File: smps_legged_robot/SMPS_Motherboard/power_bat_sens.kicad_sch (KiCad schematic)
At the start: 4 parts, among them IC2001 INA239AQDGSRQ1

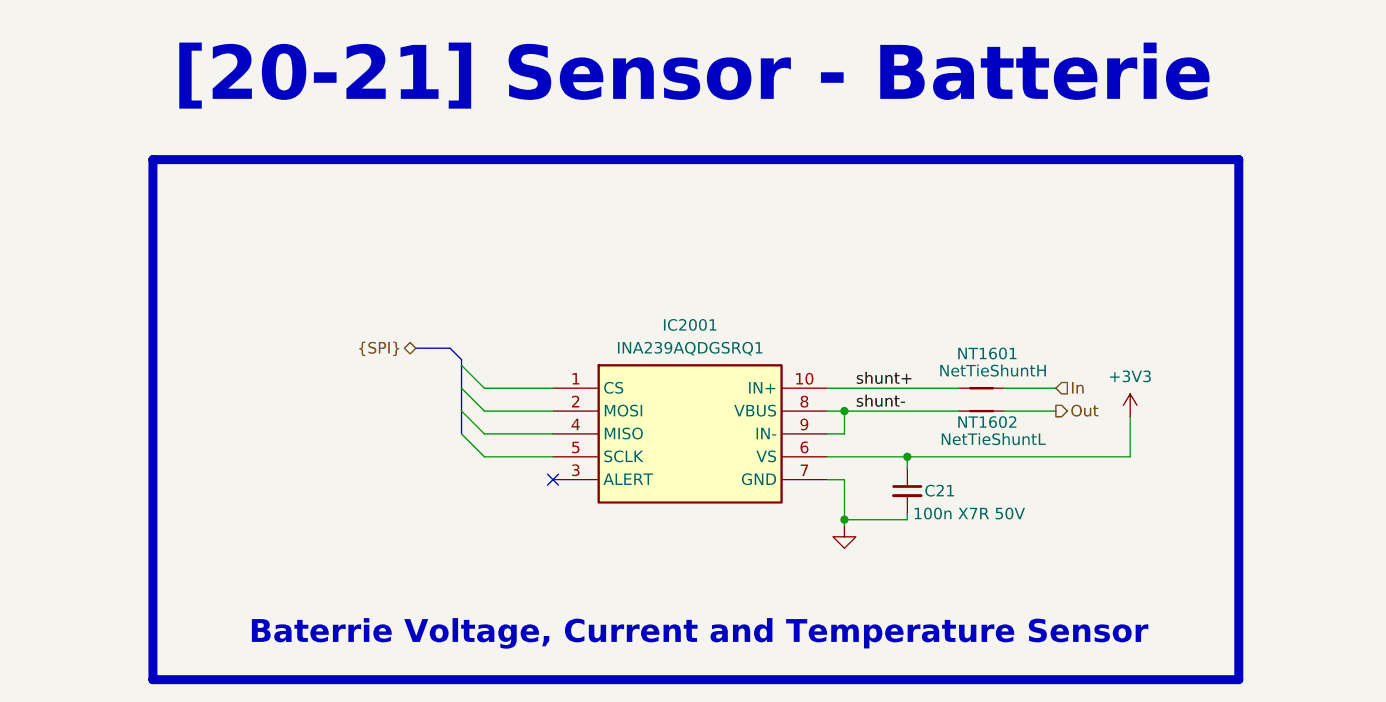
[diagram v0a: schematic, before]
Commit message: Rev 1.0 of smps finished -> waiting for verification
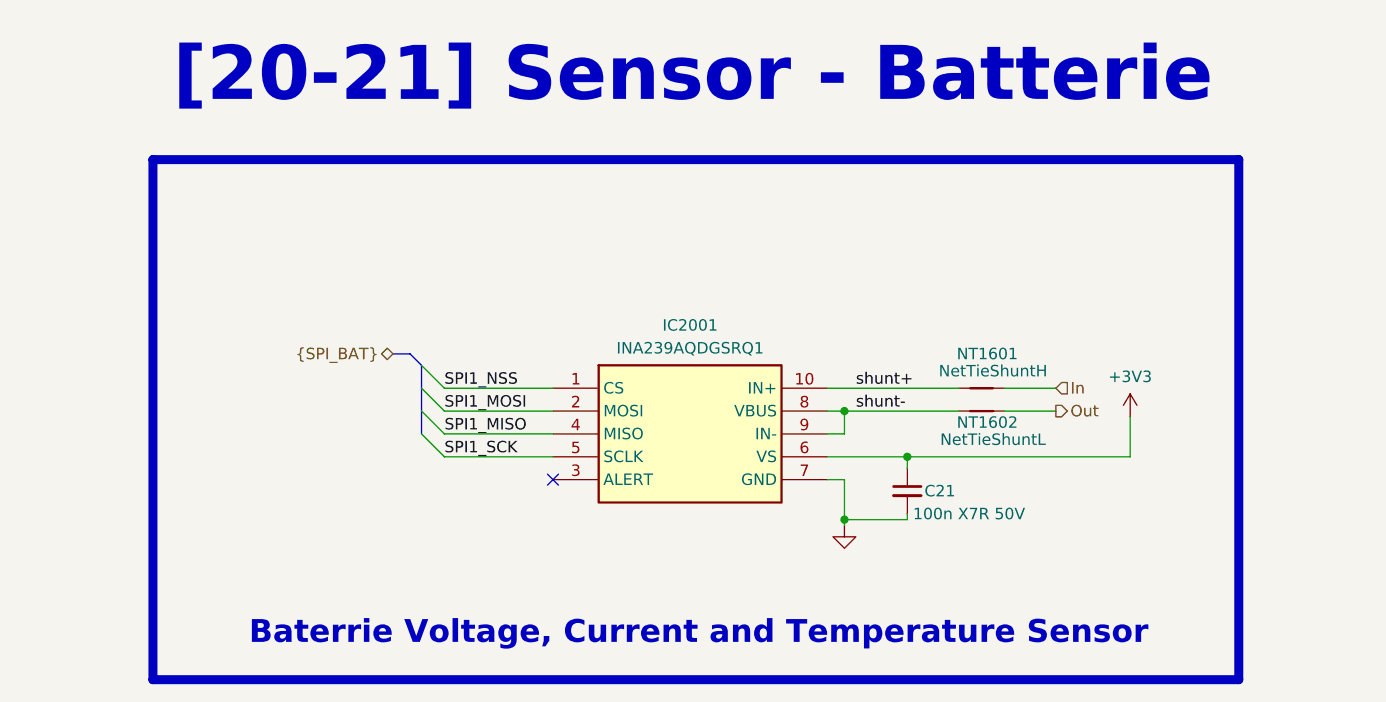
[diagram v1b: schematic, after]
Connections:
- net SPI1_NSS: now reaches IC2001.1 (CS)
- net SPI1_MOSI: now reaches IC2001.2 (MOSI)
- net SPI1_MISO: now reaches IC2001.4 (MISO)
- net SPI1_SCK: now reaches IC2001.5 (SCLK)
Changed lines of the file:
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@@
   )
   (no_connect (at 89.535 66.04))
-  (bus_entry (at 79.375 55.88) (size 2.54 2.54)
+  (bus_entry (at 74.93 53.34) (size 2.54 2.54)
     (stroke (width 0) (type default))
   )
-  (bus_entry (at 79.375 53.34) (size 2.54 2.54)
+  (bus_entry (at 74.93 60.96) (size 2.54 2.54)
     (stroke (width 0) (type default))
   )
-  (bus_entry (at 79.375 58.42) (size 2.54 2.54)
+  (bus_entry (at 74.93 58.42) (size 2.54 2.54)
     (stroke (width 0) (type default))
   )
-  (bus_entry (at 79.375 60.96) (size 2.54 2.54)
+  (bus_entry (at 74.93 55.88) (size 2.54 2.54)
     (stroke (width 0) (type default))
   )
@@
     (stroke (width 0) (type default))
   )
-  (bus (pts (xy 79.375 52.705) (xy 79.375 53.34))
-    (stroke (width 0) (type default))
-  )
-  (bus (pts (xy 79.375 53.34) (xy 79.375 55.88))
+  (bus (pts (xy 73.66 52.07) (xy 71.755 52.07))
     (stroke (width 0) (type default))
   )
@@
     (stroke (width 0) (type default))
   )
+  (bus (pts (xy 74.93 53.34) (xy 73.66 52.07))
+    (stroke (width 0) (type default))
+  )
   (wire (pts (xy 120.015 55.88) (xy 134.62 55.88))
     (stroke (width 0) (type default))
   )
-  (bus (pts (xy 79.375 55.88) (xy 79.375 58.42))
+  (wire (pts (xy 77.47 60.96) (xy 89.535 60.96))
     (stroke (width 0) (type default))
   )
-  (wire (pts (xy 81.915 60.96) (xy 89.535 60.96))
+  (bus (pts (xy 74.93 55.88) (xy 74.93 58.42))
     (stroke (width 0) (type default))
   )
@@
     (stroke (width 0) (type default))
   )
+  (wire (pts (xy 77.47 58.42) (xy 89.535 58.42))
+    (stroke (width 0) (type default))
+  )
   (wire (pts (xy 121.92 70.485) (xy 121.92 71.12))
     (stroke (width 0) (type default))
   )
-  (wire (pts (xy 81.915 55.88) (xy 89.535 55.88))
+  (wire (pts (xy 77.47 55.88) (xy 89.535 55.88))
     (stroke (width 0) (type default))
   )
   (wire (pts (xy 120.015 60.96) (xy 121.92 60.96))
-    (stroke (width 0) (type default))
-  )
-  (bus (pts (xy 79.375 58.42) (xy 79.375 60.96))
     (stroke (width 0) (type default))
   )
@@
     (stroke (width 0) (type default))
   )
-  (wire (pts (xy 81.915 58.42) (xy 89.535 58.42))
-    (stroke (width 0) (type default))
-  )
-  (bus (pts (xy 74.295 51.435) (xy 78.105 51.435))
-    (stroke (width 0) (type default))
-  )
-  (bus (pts (xy 78.105 51.435) (xy 79.375 52.705))
+  (bus (pts (xy 74.93 58.42) (xy 74.93 60.96))
     (stroke (width 0) (type default))
   )
@@
     (stroke (width 0) (type default))
   )
+  (bus (pts (xy 74.93 53.34) (xy 74.93 55.88))
+    (stroke (width 0) (type default))
+  )
   (wire (pts (xy 128.905 69.85) (xy 128.905 70.485))
     (stroke (width 0) (type default))
@@
     (stroke (width 0) (type default))
   )
-  (wire (pts (xy 81.915 63.5) (xy 89.535 63.5))
+  (wire (pts (xy 77.47 63.5) (xy 89.535 63.5))
     (stroke (width 0) (type default))
   )
@@
     (effects (font (size 1.27 1.27)) (justify left bottom))
   )
+  (label "SPI1_NSS" (at 77.47 55.88 0) (fields_autoplaced)
+    (effects (font (size 1.27 1.27)) (justify left bottom))
+  )
+  (label "SPI1_SCK" (at 77.47 63.5 0) (fields_autoplaced)
+    (effects (font (size 1.27 1.27)) (justify left bottom))
+  )
   (label "shunt-" (at 123.19 58.42 0) (fields_autoplaced)
     (effects (font (size 1.27 1.27)) (justify left bottom))
+  )
+  (label "SPI1_MOSI" (at 77.47 58.42 0) (fields_autoplaced)
+    (effects (font (size 1.27 1.27)) (justify left bottom))
+  )
+  (label "SPI1_MISO" (at 77.47 60.96 0) (fields_autoplaced)
+    (effects (font (size 1.27 1.27)) (justify left bottom))
+  )
+  (hierarchical_label "{SPI_BAT}" (shape bidirectional) (at 71.755 52.07 180) (fields_autoplaced)
+    (effects (font (size 1.27 1.27)) (justify right))
   )
   (hierarchical_label "In" (shape input) (at 145.415 55.88 0) (fields_autoplaced)
     (effects (font (size 1.27 1.27)) (justify left))
   )
-  (hierarchical_label "{SPI}" (shape bidirectional) (at 74.295 51.435 180) (fields_autoplaced)
-    (effects (font (size 1.27 1.27)) (justify right))
-  )
   (hierarchical_label "Out" (shape output) (at 145.415 58.42 0) (fields_autoplaced)

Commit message: Geode test board ready to order
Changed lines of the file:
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@@
     (effects (font (face "Times New Roman") (size 2.54 2.54) (thickness 0.508) bold (color 162 22 34 1)) (justify bottom))
   )
-  (text_box "[20-21] Sensor - Batterie"
+  (text_box "[20] Sensor - Battery\n"
     (at 12.065 14.605 0) (size 186.055 12.7)
     (stroke (width -0.0001) (type default))
